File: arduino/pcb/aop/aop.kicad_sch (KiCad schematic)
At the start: 10 parts, among them M1 RFID-RC522, Q1 AO4435, SW1 SW_Push, U1 ESP32-C3_SUPERMINI_TH, U2 TC00500

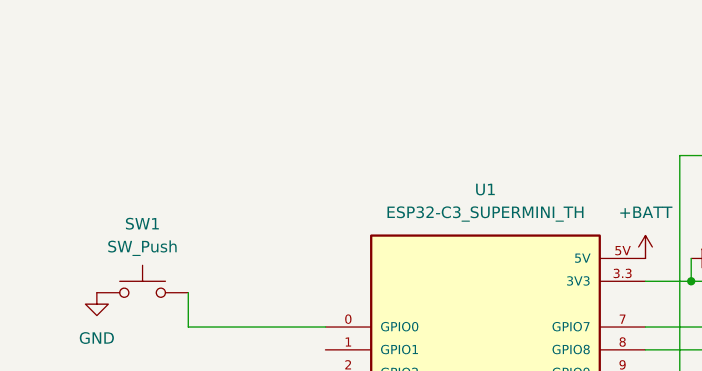
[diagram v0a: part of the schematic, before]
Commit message: PCB: start tracing
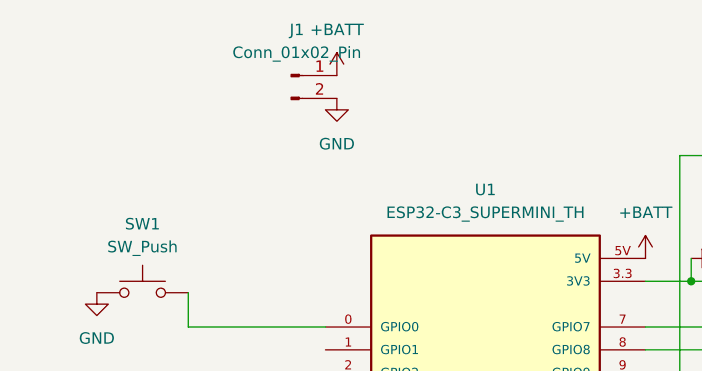
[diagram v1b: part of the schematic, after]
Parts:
- added J1: Conn_01x02_Pin, Connector_JST:JST_XH_B2B-XH-A_1x02_P2.50mm_Vertical, symbol Connector:Conn_01x02_Pin
- BZ1: footprint (none) -> Buzzer_Beeper:Buzzer_12x9.5RM7.6
- D1: footprint (none) -> LED_THT:LED_D3.0mm
- R1, R2, R3: footprint (none) -> Resistor_THT:R_Axial_DIN0207_L6.3mm_D2.5mm_P10.16mm_Horizontal
- SW1: footprint (none) -> Resistor_THT:R_Axial_DIN0614_L14.3mm_D5.7mm_P20.32mm_Horizontal
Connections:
- net +BATT: now also J1.1 (Pin_1)
- net GND: now also J1.2 (Pin_2)
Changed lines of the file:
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@@
 			)
 		)
-		(property "Footprint" ""
+		(property "Footprint" "Resistor_THT:R_Axial_DIN0207_L6.3mm_D2.5mm_P10.16mm_Horizontal"
 			(at 41.402 91.44 90)
 			(effects
@@
 				(path "/6c2f9cd3-2815-4cb2-b88c-9d452fcffe7c"
 					(reference "#PWR02")
+					(unit 1)
+				)
+			)
+		)
+	)
+	(symbol
+		(lib_id "power:GND")
+		(at 76.2 57.15 0)
+		(unit 1)
+		(exclude_from_sim no)
+		(in_bom yes)
+		(on_board yes)
+		(dnp no)
+		(fields_autoplaced yes)
+		(property "Reference" "#PWR011"
+			(at 76.2 63.5 0)
+			(effects
+				(font
+					(size 1.27 1.27)
+				)
+				(hide yes)
+			)
+		)
+		(property "Value" "GND"
+			(at 76.2 62.23 0)
+			(effects
+				(font
+					(size 1.27 1.27)
+				)
+			)
+		)
+		(property "Footprint" ""
+			(at 76.2 57.15 0)
+			(effects
+				(font
+					(size 1.27 1.27)
+				)
+				(hide yes)
+			)
+		)
+		(property "Datasheet" ""
+			(at 76.2 57.15 0)
+			(effects
+				(font
+					(size 1.27 1.27)
+				)
+				(hide yes)
+			)
+		)
+		(property "Description" "Power symbol creates a global label with name \"GND\" , ground"
+			(at 76.2 57.15 0)
+			(effects
+				(font
+					(size 1.27 1.27)
+				)
+				(hide yes)
+			)
+		)
+		(pin "1"
+		)
+		(instances
+			(project ""
+				(path "/6c2f9cd3-2815-4cb2-b88c-9d452fcffe7c"
+					(reference "#PWR011")
 					(unit 1)
 				)
@@
 			)
 		)
-		(property "Footprint" ""
+		(property "Footprint" "Resistor_THT:R_Axial_DIN0207_L6.3mm_D2.5mm_P10.16mm_Horizontal"
 			(at 123.952 71.12 90)
 			(effects
@@
 			)
 		)
-		(property "Footprint" ""
+		(property "Footprint" "Buzzer_Beeper:Buzzer_12x9.5RM7.6"
 			(at 60.325 90.17 90)
 			(effects
@@
 			)
 		)
-		(property "Footprint" ""
+		(property "Footprint" "Resistor_THT:R_Axial_DIN0614_L14.3mm_D5.7mm_P20.32mm_Horizontal"
 			(at 54.61 73.66 0)
 			(effects
@@
 	)
 	(symbol
+		(lib_id "Connector:Conn_01x02_Pin")
+		(at 71.12 54.61 0)
+		(unit 1)
+		(exclude_from_sim no)
+		(in_bom yes)
+		(on_board yes)
+		(dnp no)
+		(fields_autoplaced yes)
+		(property "Reference" "J1"
+			(at 71.755 49.53 0)
+			(effects
+				(font
+					(size 1.27 1.27)
+				)
+			)
+		)
+		(property "Value" "Conn_01x02_Pin"
+			(at 71.755 52.07 0)
+			(effects
+				(font
+					(size 1.27 1.27)
+				)
+			)
+		)
+		(property "Footprint" "Connector_JST:JST_XH_B2B-XH-A_1x02_P2.50mm_Vertical"
+			(at 71.12 54.61 0)
+			(effects
+				(font
+					(size 1.27 1.27)
+				)
+				(hide yes)
+			)
+		)
+		(property "Datasheet" "~"
+			(at 71.12 54.61 0)
+			(effects
+				(font
+					(size 1.27 1.27)
+				)
+				(hide yes)
+			)
+		)
+		(property "Description" "Generic connector, single row, 01x02, script generated"
+			(at 71.12 54.61 0)
+			(effects
+				(font
+					(size 1.27 1.27)
+				)
+				(hide yes)
+			)
+		)
+		(pin "1"
+		)
+		(pin "2"
+		)
+		(instances
+			(project ""
+				(path "/6c2f9cd3-2815-4cb2-b88c-9d452fcffe7c"
+					(reference "J1")
+					(unit 1)
+				)
+			)
+		)
+	)
+	(symbol
 		(lib_id "power:+3.3VA")
 		(at 134.62 67.31 0)
@@
 	)
 	(symbol
+		(lib_id "power:+BATT")
+		(at 76.2 54.61 0)
+		(unit 1)
+		(exclude_from_sim no)
+		(in_bom yes)
+		(on_board yes)
+		(dnp no)
+		(fields_autoplaced yes)
+		(property "Reference" "#PWR012"
+			(at 76.2 58.42 0)
+			(effects
+				(font
+					(size 1.27 1.27)
+				)
+				(hide yes)
+			)
+		)
+		(property "Value" "+BATT"
+			(at 76.2 49.53 0)
+			(effects
+				(font
+					(size 1.27 1.27)
+				)
+			)
+		)
+		(property "Footprint" ""
+			(at 76.2 54.61 0)
+			(effects
+				(font
+					(size 1.27 1.27)
+				)
+				(hide yes)
+			)
+		)
+		(property "Datasheet" ""
+			(at 76.2 54.61 0)
+			(effects
+				(font
+					(size 1.27 1.27)
+				)
+				(hide yes)
+			)
+		)
+		(property "Description" "Power symbol creates a global label with name \"+BATT\""
+			(at 76.2 54.61 0)
+			(effects
+				(font
+					(size 1.27 1.27)
+				)
+				(hide yes)
+			)
+		)
+		(pin "1"
+		)
+		(instances
+			(project ""
+				(path "/6c2f9cd3-2815-4cb2-b88c-9d452fcffe7c"
+					(reference "#PWR012")
+					(unit 1)
+				)
+			)
+		)
+	)
+	(symbol
 		(lib_id "RFID-RC522:RFID-RC522")
 		(at 143.51 120.65 0)
@@
 			)
 		)
-		(property "Footprint" ""
+		(property "Footprint" "LED_THT:LED_D3.0mm"
 			(at 43.18 99.06 0)
 			(effects
@@
 			)
 		)
-		(property "Footprint" ""
+		(property "Footprint" "Resistor_THT:R_Axial_DIN0207_L6.3mm_D2.5mm_P10.16mm_Horizontal"
 			(at 119.38 73.152 90)
 			(effects

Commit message: Try two-layer PCB
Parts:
- SW1: footprint Resistor_THT:R_Axial_DIN0614_L14.3mm_D5.7mm_P20.32mm_Horizontal -> Resistor_THT:R_Axial_DIN0414_L11.9mm_D4.5mm_P15.24mm_Horizontal
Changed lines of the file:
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@@
 			)
 		)
-		(property "Footprint" "Resistor_THT:R_Axial_DIN0614_L14.3mm_D5.7mm_P20.32mm_Horizontal"
+		(property "Footprint" "Resistor_THT:R_Axial_DIN0414_L11.9mm_D4.5mm_P15.24mm_Horizontal"
 			(at 54.61 73.66 0)
 			(effects

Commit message: [arduino] Update schematics
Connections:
- net +BATT: now also BZ1.1 (+), D1.1 (K), Q1.1, Q1.2, Q1.3, R1.2, U1.3.3 (3V3); no longer U1.5V
- net GND: no longer BZ1.2 (-), D1.1 (K)
- net at U1.1 (GPIO1): now also M1.5 (IRQ)
- net at U1.21 (GPIO21): now also R2.2; no longer R2.1
- net at U1.3 (GPIO3): now also BZ1.2 (-); no longer BZ1.1 (+)
- net at Q1.4, R1.1: now also R2.1; no longer R2.2
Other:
- moved on the sheet: BZ1, D1, R2, R3

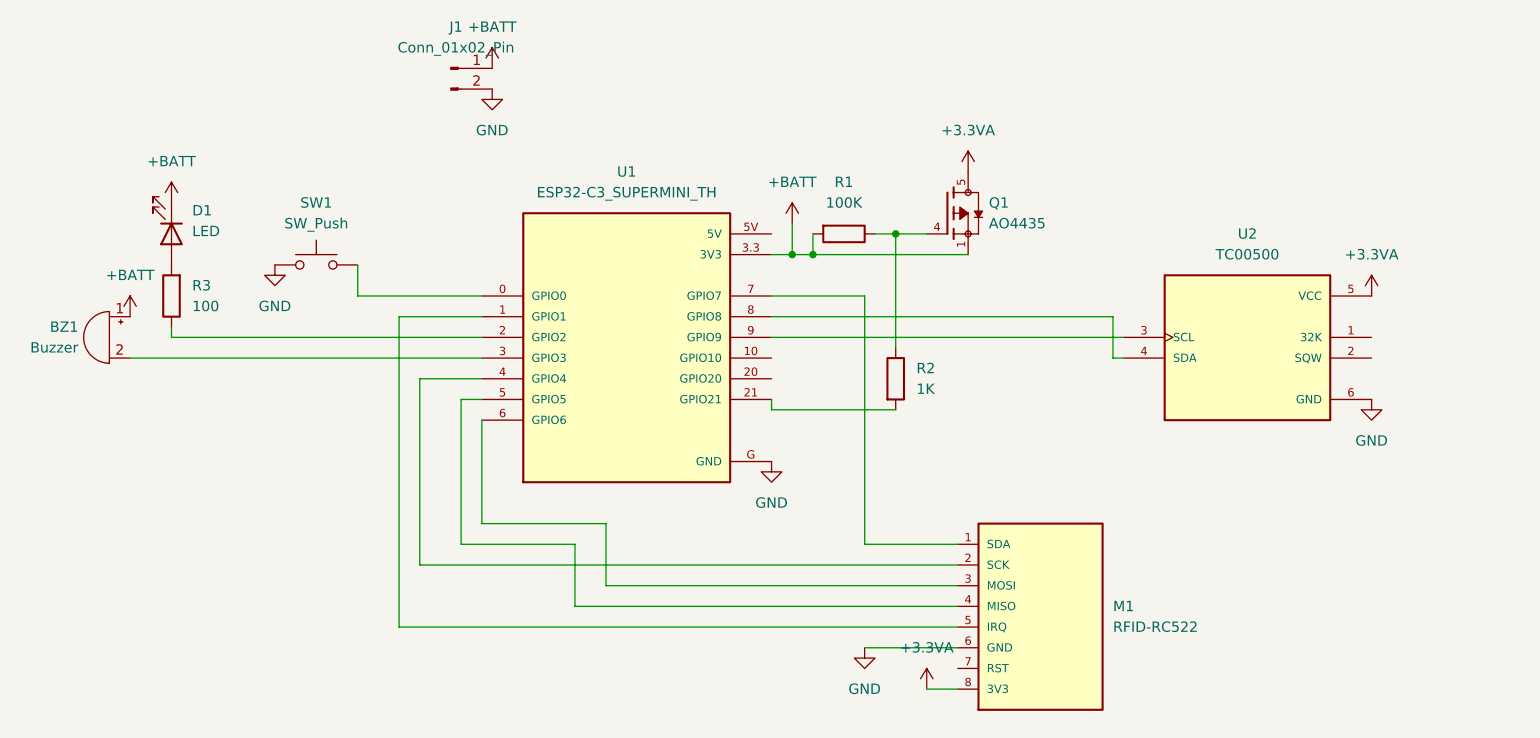
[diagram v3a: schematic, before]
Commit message: Remove DS3231
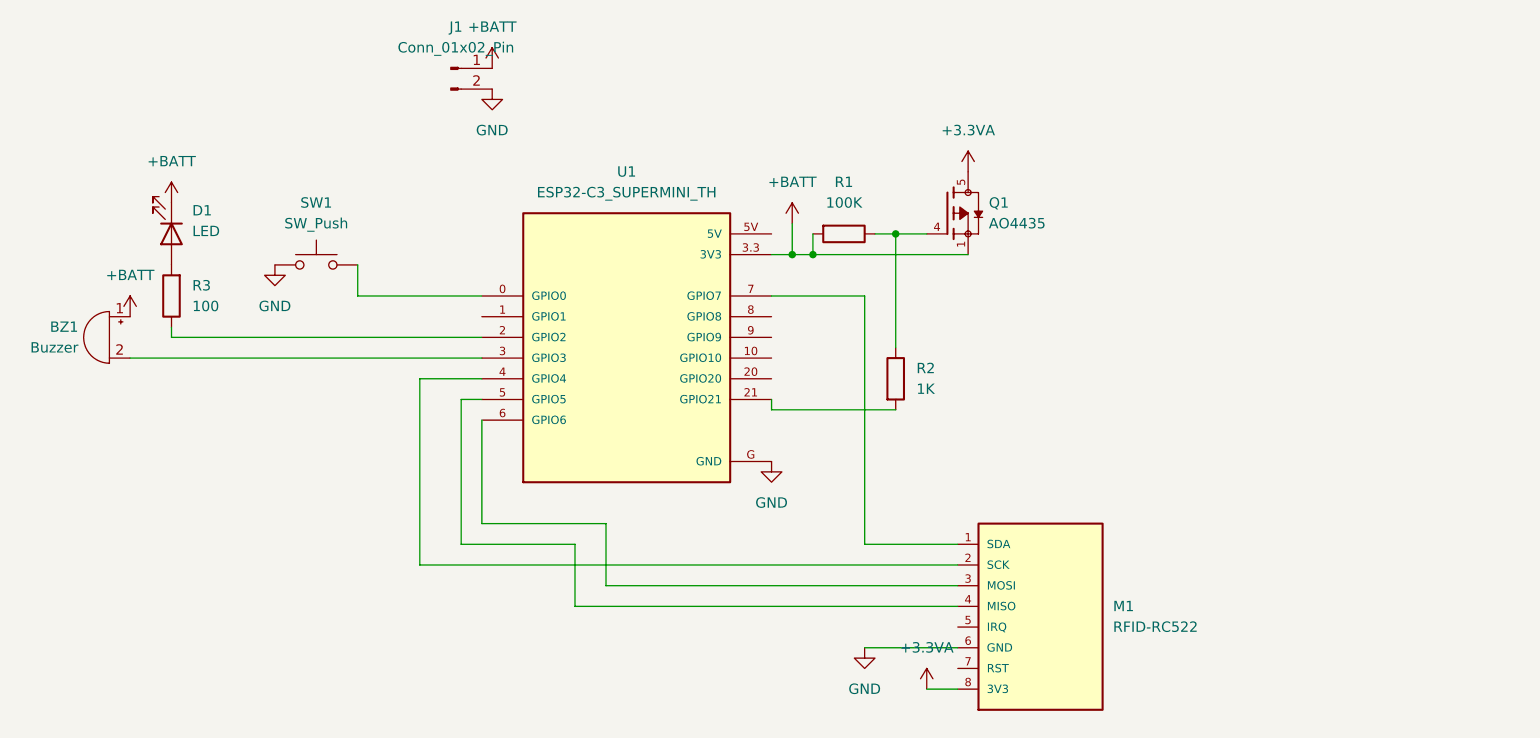
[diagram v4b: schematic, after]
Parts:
- removed U2: TC00500, TC00500:MODULE_TC00500, symbol TC00500:TC00500
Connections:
- net at U1.1 (GPIO1): no longer M1.5 (IRQ)

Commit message: [pcb] Add one more wakeup switch
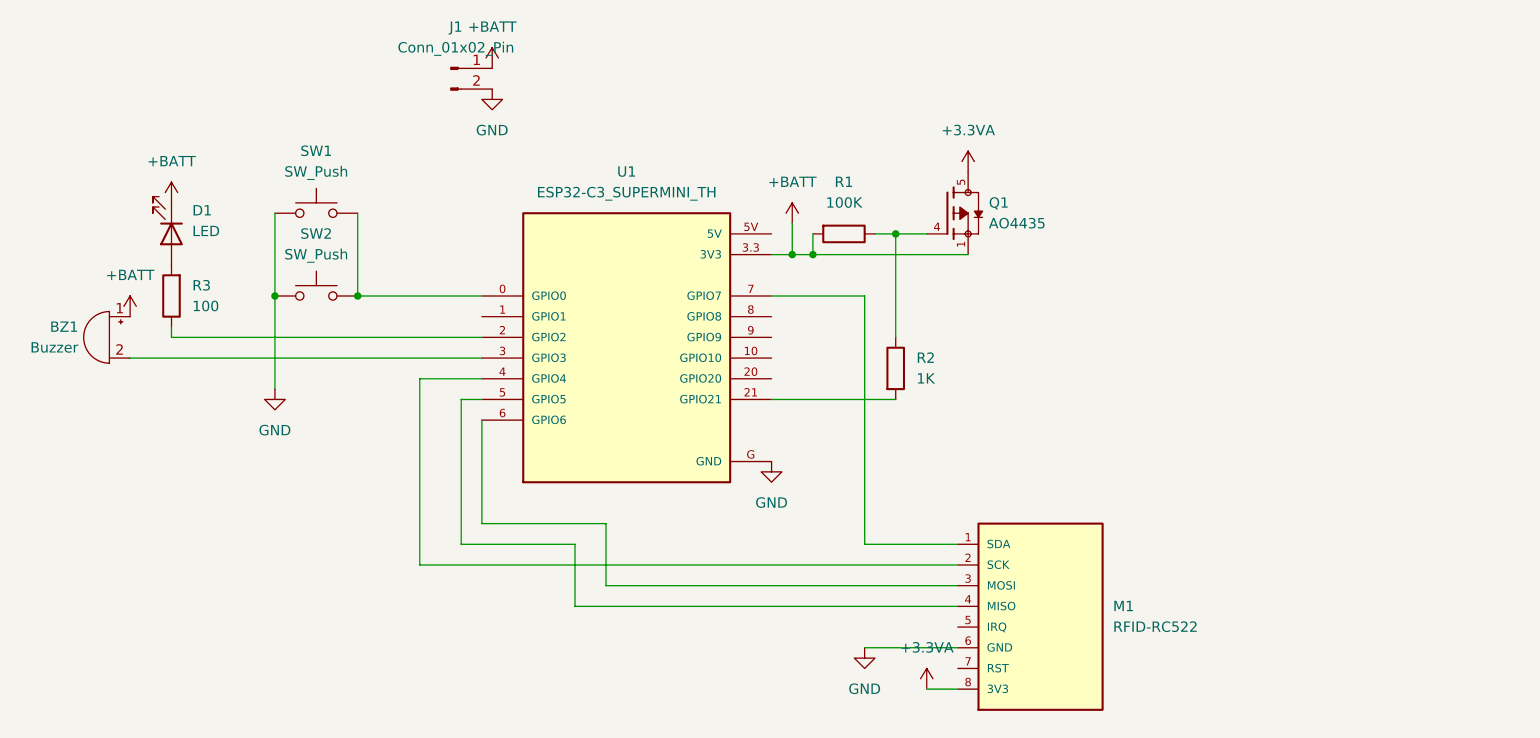
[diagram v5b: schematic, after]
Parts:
- added SW2: SW_Push, Resistor_THT:R_Axial_DIN0414_L11.9mm_D4.5mm_P15.24mm_Horizontal, symbol Switch:SW_Push
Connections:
- net GND: now also SW2.1
- net at SW1.2, U1.0 (GPIO0): now also SW2.2
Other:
- moved on the sheet: R2, SW1
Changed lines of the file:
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@@
 	(paper "A4")
+	(junction
+		(at 59.69 82.55)
+		(diameter 0)
+		(color 0 0 0 0)
+	)
 	(junction
 		(at 125.73 74.93)
@@
 	)
 	(junction
+		(at 49.53 82.55)
+		(diameter 0)
+		(color 0 0 0 0)
+	)
+	(junction
 		(at 115.57 77.47)
 		(diameter 0)
@@
 	(wire
 		(pts
+			(xy 49.53 93.98) (xy 49.53 82.55)
+		)
+		(stroke
+			(width 0)
+			(type default)
+		)
+	)
+	(wire
+		(pts
 			(xy 72.39 95.25) (xy 74.93 95.25)
 		)
@@
 	(wire
 		(pts
+			(xy 49.53 82.55) (xy 49.53 72.39)
+		)
+		(stroke
+			(width 0)
+			(type default)
+		)
+	)
+	(wire
+		(pts
 			(xy 121.92 113.03) (xy 133.35 113.03)
 		)
@@
 	(wire
 		(pts
-			(xy 110.49 95.25) (xy 110.49 96.52)
-		)
-		(stroke
-			(width 0)
-			(type default)
-		)
-	)
-	(wire
-		(pts
 			(xy 74.93 110.49) (xy 74.93 97.79)
 		)
@@
 	(wire
 		(pts
-			(xy 110.49 96.52) (xy 125.73 96.52)
+			(xy 110.49 95.25) (xy 125.73 95.25)
 		)
 		(stroke
@@
 	(wire
 		(pts
-			(xy 125.73 74.93) (xy 125.73 88.9)
-		)
-		(stroke
-			(width 0)
-			(type default)
-		)
-	)
-	(wire
-		(pts
-			(xy 59.69 78.74) (xy 59.69 82.55)
+			(xy 125.73 74.93) (xy 125.73 87.63)
+		)
+		(stroke
+			(width 0)
+			(type default)
+		)
+	)
+	(wire
+		(pts
+			(xy 59.69 72.39) (xy 59.69 82.55)
 		)
 		(stroke
@@
 	)
 	(symbol
+		(lib_id "Switch:SW_Push")
+		(at 54.61 82.55 0)
+		(unit 1)
+		(exclude_from_sim no)
+		(in_bom yes)
+		(on_board yes)
+		(dnp no)
+		(fields_autoplaced yes)
+		(property "Reference" "SW2"
+			(at 54.61 74.93 0)
+			(effects
+				(font
+					(size 1.27 1.27)
+				)
+			)
+		)
+		(property "Value" "SW_Push"
+			(at 54.61 77.47 0)
+			(effects
+				(font
+					(size 1.27 1.27)
+				)
+			)
+		)
+		(property "Footprint" "Resistor_THT:R_Axial_DIN0414_L11.9mm_D4.5mm_P15.24mm_Horizontal"
+			(at 54.61 77.47 0)
+			(effects
+				(font
+					(size 1.27 1.27)
+				)
+				(hide yes)
+			)
+		)
+		(property "Datasheet" "~"
+			(at 54.61 77.47 0)
+			(effects
+				(font
+					(size 1.27 1.27)
+				)
+				(hide yes)
+			)
+		)
+		(property "Description" "Push button switch, generic, two pins"
+			(at 54.61 82.55 0)
+			(effects
+				(font
+					(size 1.27 1.27)
+				)
+				(hide yes)
+			)
+		)
+		(pin "1"
+		)
+		(pin "2"
+		)
+		(instances
+			(project "aop"
+				(path "/6c2f9cd3-2815-4cb2-b88c-9d452fcffe7c"
+					(reference "SW2")
+					(unit 1)
+				)
+			)
+		)
+	)
+	(symbol
 		(lib_id "ESP32-C3_SUPERMINI_TH:ESP32-C3_SUPERMINI_TH")
 		(at 92.71 87.63 0)
@@
 	(symbol
 		(lib_id "Device:R")
-		(at 125.73 92.71 0)
+		(at 125.73 91.44 0)
 		(unit 1)
 		(exclude_from_sim no)
@@
 		(fields_autoplaced yes)
 		(property "Reference" "R2"
-			(at 128.27 91.4399 0)
+			(at 128.27 90.1699 0)
 			(effects
 				(font
@@
 		)
 		(property "Value" "1K"
-			(at 128.27 93.9799 0)
+			(at 128.27 92.7099 0)
 			(effects
 				(font
@@
 		)
 		(property "Footprint" "Resistor_THT:R_Axial_DIN0207_L6.3mm_D2.5mm_P10.16mm_Horizontal"
-			(at 123.952 92.71 90)
+			(at 123.952 91.44 90)
 			(effects
 				(font
@@
 		)
 		(property "Datasheet" "~"
-			(at 125.73 92.71 0)
+			(at 125.73 91.44 0)
 			(effects
 				(font
@@
 		)
 		(property "Description" "Resistor"
-			(at 125.73 92.71 0)
+			(at 125.73 91.44 0)
 			(effects
 				(font
@@
 	(symbol
 		(lib_id "Switch:SW_Push")
-		(at 54.61 78.74 0)
+		(at 54.61 72.39 0)
 		(unit 1)
 		(exclude_from_sim no)
@@
 		(fields_autoplaced yes)
 		(property "Reference" "SW1"
-			(at 54.61 71.12 0)
+			(at 54.61 64.77 0)
 			(effects
 				(font
@@
 		)
 		(property "Value" "SW_Push"
-			(at 54.61 73.66 0)
+			(at 54.61 67.31 0)
 			(effects
 				(font
@@
 		)
 		(property "Footprint" "Resistor_THT:R_Axial_DIN0414_L11.9mm_D4.5mm_P15.24mm_Horizontal"
-			(at 54.61 73.66 0)
+			(at 54.61 67.31 0)
 			(effects
 				(font
@@
 		)
 		(property "Datasheet" "~"
-			(at 54.61 73.66 0)
+			(at 54.61 67.31 0)
 			(effects
 				(font
@@
 		)
 		(property "Description" "Push button switch, generic, two pins"
-			(at 54.61 78.74 0)
+			(at 54.61 72.39 0)
 			(effects
 				(font
@@
 	(symbol
 		(lib_id "power:GND")
-		(at 49.53 78.74 0)
+		(at 49.53 93.98 0)
 		(unit 1)
 		(exclude_from_sim no)
@@
 		(fields_autoplaced yes)
 		(property "Reference" "#PWR010"
-			(at 49.53 85.09 0)
+			(at 49.53 100.33 0)
 			(effects
 				(font
@@
 		)
 		(property "Value" "GND"
-			(at 49.53 83.82 0)
+			(at 49.53 99.06 0)
 			(effects
 				(font
@@
 		)
 		(property "Footprint" ""
-			(at 49.53 78.74 0)
+			(at 49.53 93.98 0)
 			(effects
 				(font
@@
 		)
 		(property "Datasheet" ""
-			(at 49.53 78.74 0)
+			(at 49.53 93.98 0)
 			(effects
 				(font
@@
 		)
 		(property "Description" "Power symbol creates a global label with name \"GND\" , ground"
-			(at 49.53 78.74 0)
-			(effects
-				(font
+			(at 49.53 93.98 0)
+			(effects
+				(font
